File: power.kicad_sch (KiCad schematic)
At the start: 7 parts, among them U3 AP2112K-3.3, U4 SC189CSKTRT

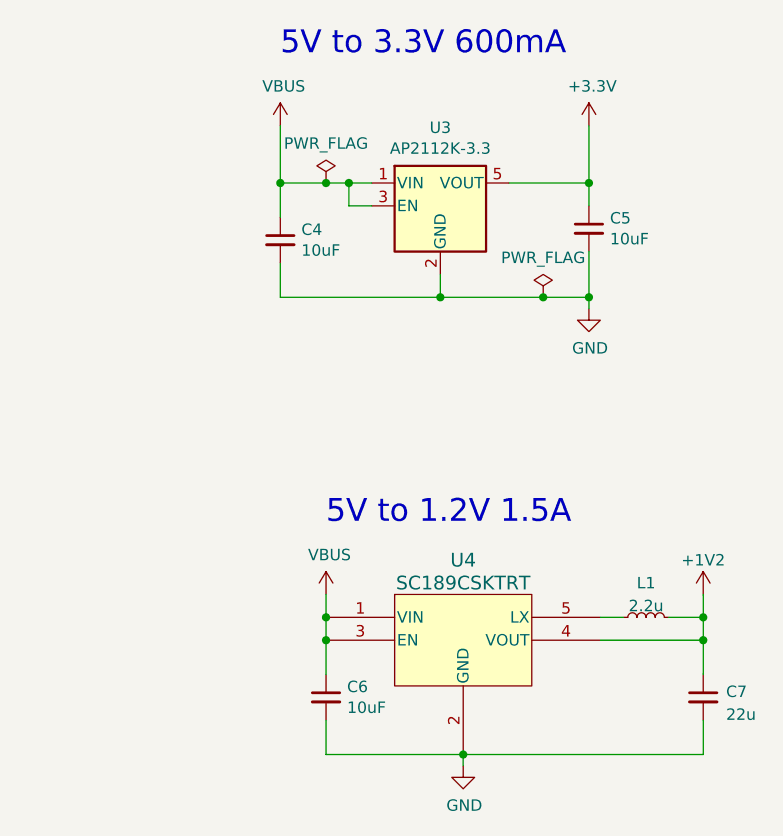
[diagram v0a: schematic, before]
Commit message: update to kicad 9
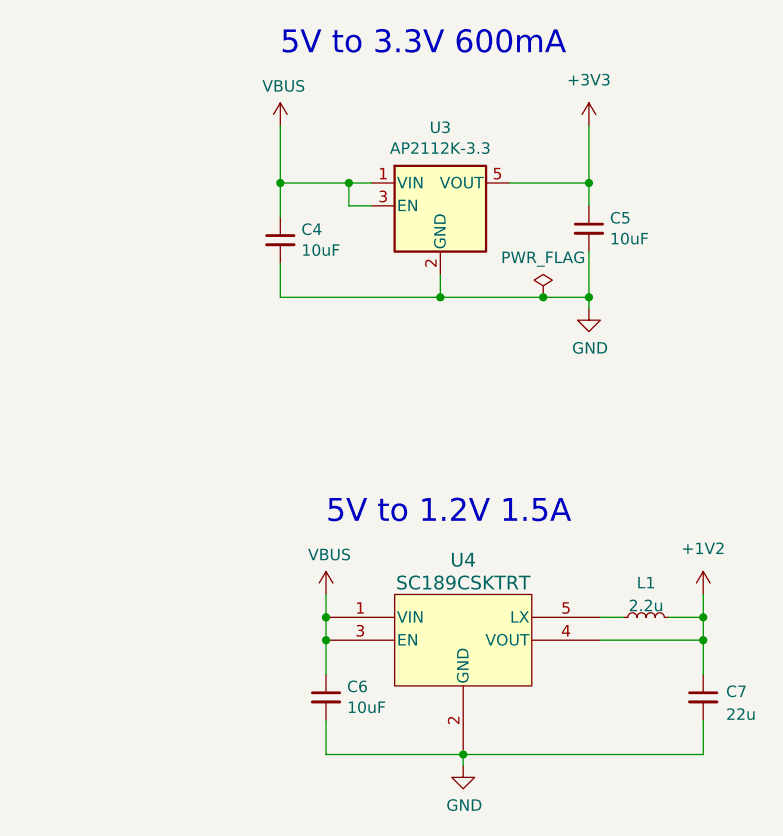
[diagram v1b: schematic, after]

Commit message: implement USB3.0 active redriver and fix DRC errors
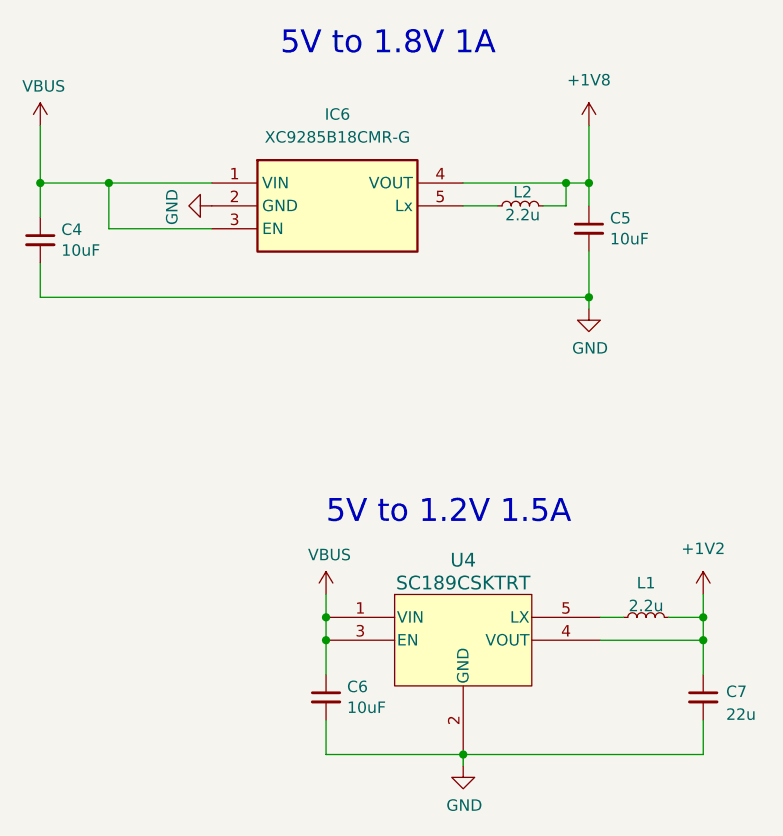
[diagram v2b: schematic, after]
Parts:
- removed U3: AP2112K-3.3, Package_TO_SOT_SMD:SOT-23-5, symbol Regulator_Linear:AP2112K-3.3
- added IC6: XC9285B18CMR-G, Samacsys:SOT95P280X130-5N, symbol Samacsys:XC9285B18CMR-G
- added L2: 2.2u, Inductor_SMD:L_1008_2520Metric, symbol Device:L_Small
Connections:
- net GND: now also IC6.2 (GND)
- net VBUS: now also IC6.1 (VIN), IC6.3 (EN)
- net +3V3 renamed +1V8
- net +1V8: now also IC6.4 (VOUT), L2.2
- new net: IC6.5 (Lx), L2.1
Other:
- note added: "5V to 1.8V 1A"
- note removed: "5V to 3.3V 600mA"
- moved on the sheet: C4

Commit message: add AC caps for redriver; fix ERC and DRC errors
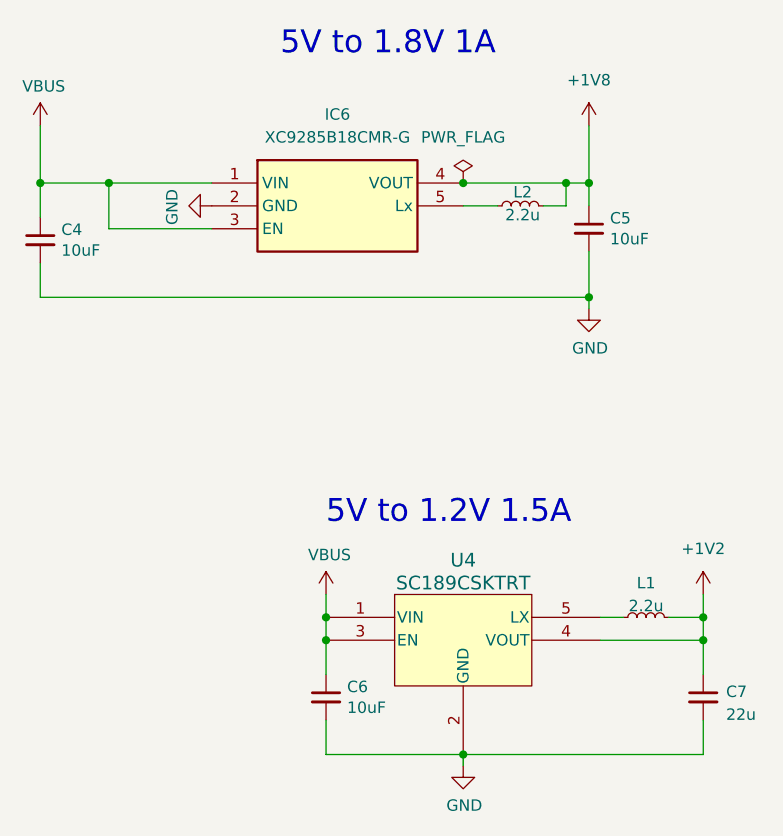
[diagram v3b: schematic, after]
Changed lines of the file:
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@@
+	)
+	(junction
+		(at 78.74 44.45)
+		(diameter 0)
+		(color 0 0 0 0)
 	)
 	(junction
@@
 					(unit 1)
 				)
+			)
+		)
+	)
+	(symbol
+		(lib_id "power:PWR_FLAG")
+		(at 78.74 44.45 0)
+		(unit 1)
+		(exclude_from_sim no)
+		(in_bom yes)
+		(on_board yes)
+		(dnp no)
+		(fields_autoplaced yes)
+		(property "Reference" "#FLG01"
+			(at 78.74 42.545 0)
+			(effects
+				(font
+					(size 1.27 1.27)
+				)
+				(hide yes)
+			)
+		)
+		(property "Value" "PWR_FLAG"
+			(at 78.74 39.37 0)
+			(effects
+				(font
+					(size 1.27 1.27)
+				)
+			)
+		)
+		(property "Footprint" ""
+			(at 78.74 44.45 0)
+			(effects
+				(font
+					(size 1.27 1.27)
+				)
+				(hide yes)
+			)
+		)
+		(property "Datasheet" "~"
+			(at 78.74 44.45 0)
+			(effects
+				(font
+					(size 1.27 1.27)
+				)
+				(hide yes)
+			)
+		)
+		(property "Description" "Special symbol for telling ERC where power comes from"
+			(at 78.74 44.45 0)
+			(effects
+				(font
+					(size 1.27 1.27)
+				)
+				(hide yes)
+			)
+		)
+		(pin "1"
+		)
+		(instances
+			(project ""
+				(path "/cec59c69-8f0d-4d06-8fee-6cd1bb72d09c/df825620-032c-4492-9362-da032e4f40e2"
+					(reference "#FLG01")
+					(unit 1)
+				)

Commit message: start implementing SML feedback
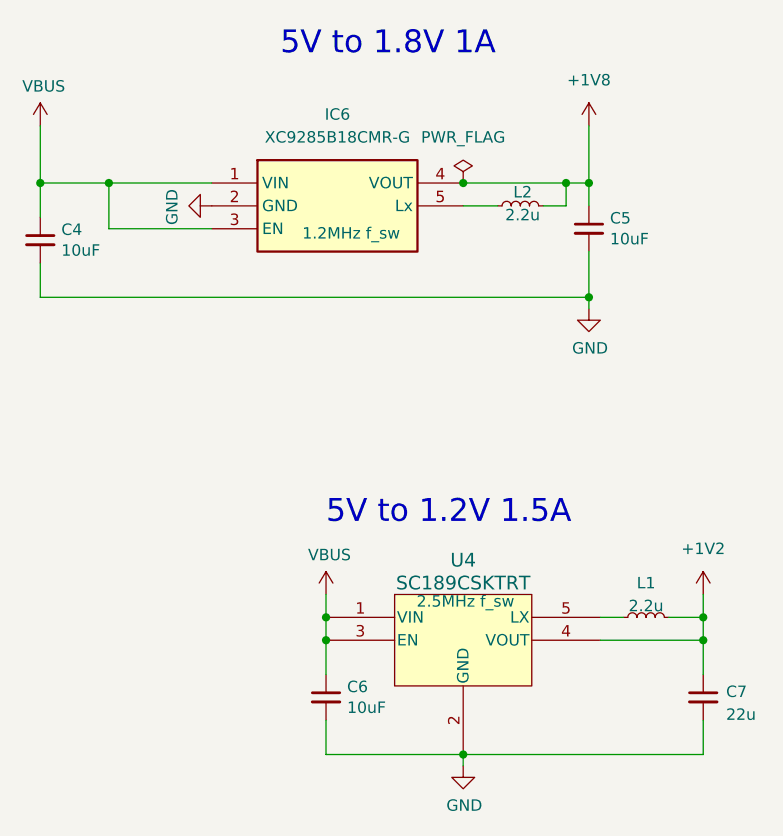
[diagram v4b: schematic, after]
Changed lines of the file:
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@@
 		(on_board yes)
 		(dnp no)
-		(fields_autoplaced yes)
 		(property "Reference" "IC6"
 			(at 64.77 36.83 0)
@@
 			)
 		)
-		(property "Description" "HiSAT-COT Control, 1A Synchronous Step-Down DC/DC Converters"
-			(at 50.8 44.45 0)
-			(effects
-				(font
-					(size 1.27 1.27)
-				)
-				(hide yes)
+		(property "Description" "1.2MHz f_sw"
+			(at 66.294 50.038 0)
+			(effects
+				(font
+					(size 1.27 1.27)
+				)
 			)
 		)
@@
 		(on_board yes)
 		(dnp no)
-		(fields_autoplaced yes)
 		(property "Reference" "U4"
 			(at 78.74 86.36 0)
@@
 			)
 		)
-		(property "Description" ""
-			(at 58.42 95.25 0)
-			(effects
-				(font
+		(property "Description" "2.5MHz f_sw"
+			(at 78.994 90.932 0)
+			(effects
+				(font
